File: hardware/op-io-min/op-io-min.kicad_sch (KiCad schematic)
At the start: 15 parts, among them J1 USB_A, J2 RUN, J3 MIDI_IN, J4 MIDI_OUT, J5 USB_HEADER, U1 Teensy4.1, U2 6N138

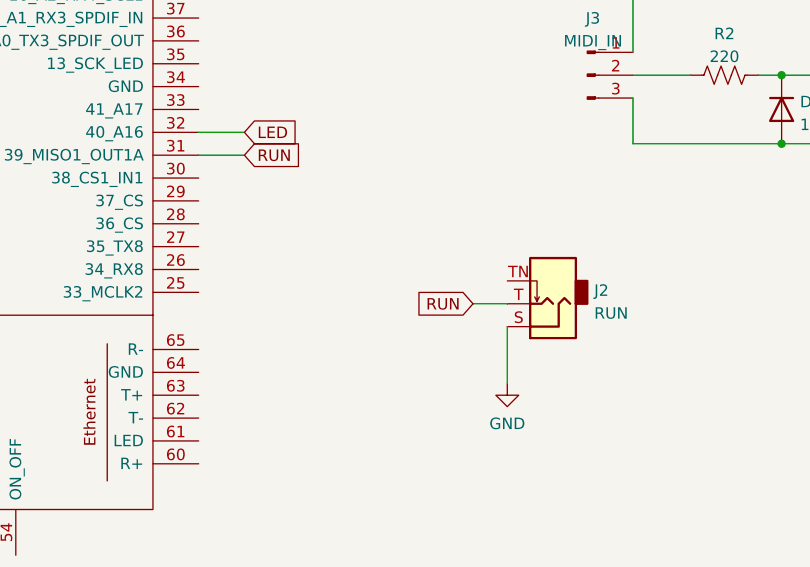
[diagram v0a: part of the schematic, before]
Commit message: added output impedance resistor
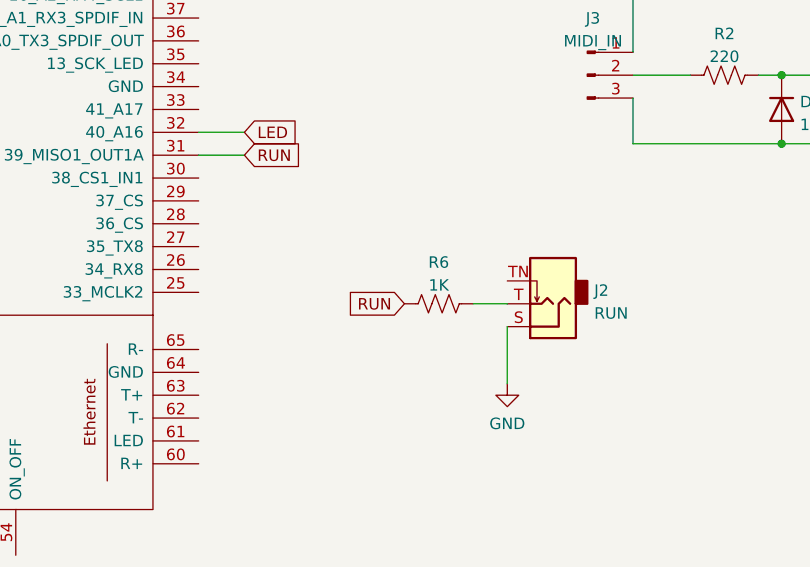
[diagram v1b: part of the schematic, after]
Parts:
- added R6: 1K, Resistor_THT:R_Axial_DIN0207_L6.3mm_D2.5mm_P7.62mm_Horizontal, symbol Device:R_US
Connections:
- net RUN: now also R6.1; no longer J2.T (Tip)
- new net: J2.T (Tip), R6.2
